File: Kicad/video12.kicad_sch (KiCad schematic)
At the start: 19 parts, among them J301 DE15HD, U301 THS7316, U302 TPD7S019

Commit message: Cleaned up the part numbers.
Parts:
- C301: Digikey 490-3886-1-ND -> (none); JLCPCB Collection (none) -> Basic; MPN GRM21BR61C106KE15L -> CL21A106KAYNNNE; Manufacturer Murata -> Samsung; Mouser 81-GRM21BR61C106KE15 -> (none); Voltage 10V -> 25V
- C302, C306: Digikey 399-C0805C104M5RAC7800CT-ND -> (none); JLCPCB Collection (none) -> Basic; MPN C0805C104M5RACTU -> CC0805KRX7R9BB104; Manufacturer Kemet -> Yageo; Mouser 80-C0805C104M5R -> (none); Tolerance X5R -> X7R; Voltage 10V -> 50V
- C303: Digikey 1276-1093-1-ND -> (none); JLCPCB Collection (none) -> Basic; Tolerance X5R -> X7R
- C304, C305: Digikey 399-C0805C104M5RAC7800CT-ND -> (none); JLCPCB Collection (none) -> Basic; MPN C0805C104M5RACTU -> CC0805KRX7R9BB104; Manufacturer Kemet -> Yageo; Mouser 80-C0805C104M5R -> (none); Tolerance X5R -> X7R; Voltage 16V -> 50V
- R301, R302, R303: Digikey RMCF0805FT75R0CT-ND -> (none); JLCPCB Collection (none) -> Basic; MPN RMCF0805FT75R0 -> 0805W8F750JT5E; Manufacturer Stackpole -> Uniroyal
- R305, R306: Digikey RMCF0805FT2K00CT-ND -> (none); JLCPCB Collection (none) -> Basic; MPN RMCF0805FT2K00 -> 0805W8F2001T5E; Manufacturer Stackpole -> Uniroyal
- U301: Digikey 296-26684-1-ND -> (none); JLCPCB Collection (none) -> Extended; MPN THS7316DR -> TPF133A; Manufacturer Texas Instruments -> 3PEAK; Mouser 595-THS7316DR -> (none)
- U302: Digikey 296-27595-1-ND -> (none); JLCPCB Collection (none) -> Extended; Mouser 595-TPD7S019-15DBQR -> (none)

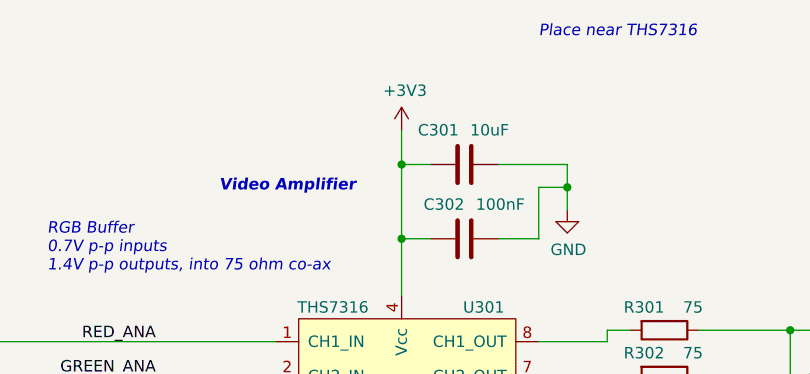
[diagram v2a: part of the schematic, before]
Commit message: Added a PC Speaker output.
To free up a BMC pin, the HDD LED is now driven from the I/O mux.
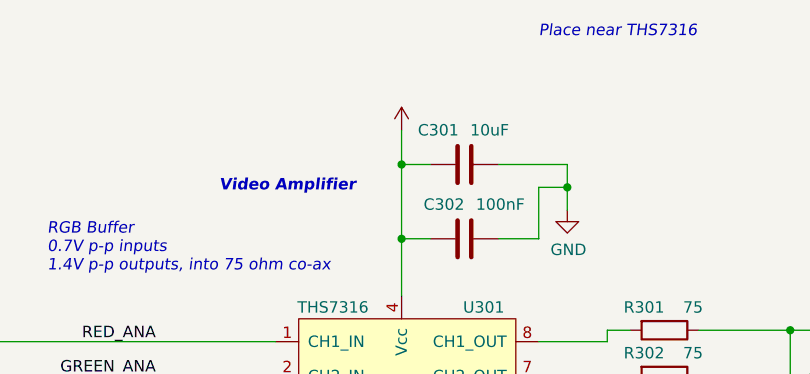
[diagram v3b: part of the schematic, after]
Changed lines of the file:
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@@
       (effects (font (size 1.27 1.27)) hide)
     )
-    (property "Value" "+3V3" (id 1) (at 110.871 41.9608 0))
+    (property "Value" "" (id 1) (at 110.871 41.9608 0))
     (property "Footprint" "" (id 2) (at 110.49 46.355 0)
       (effects (font (size 1.27 1.27)) hide)

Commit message: Label tweaks
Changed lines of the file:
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@@
       (effects (font (size 1.27 1.27)) hide)
     )
-    (property "Value" "" (id 1) (at 110.871 41.9608 0))
+    (property "Value" "+3V3" (id 1) (at 110.871 41.9608 0))
     (property "Footprint" "" (id 2) (at 110.49 46.355 0)
       (effects (font (size 1.27 1.27)) hide)

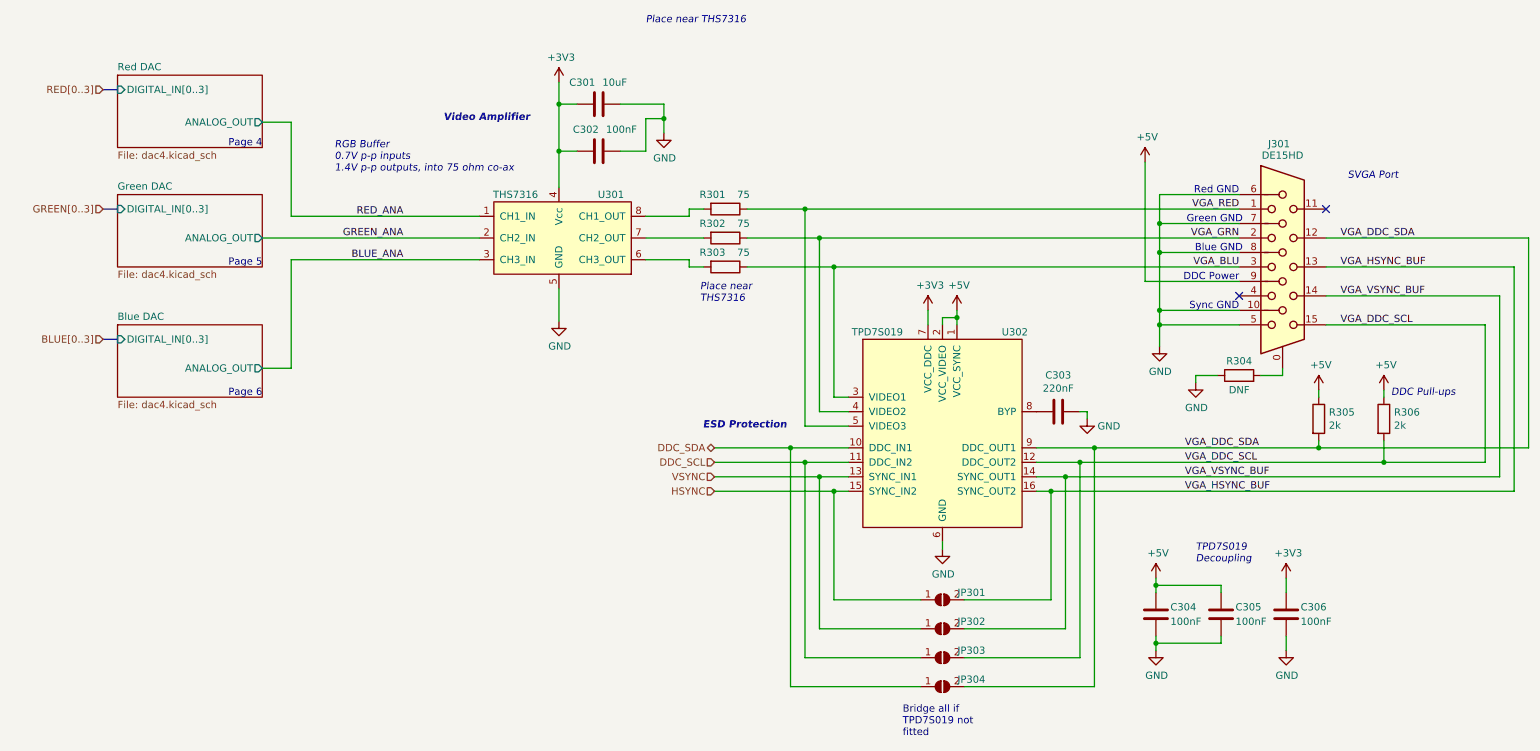
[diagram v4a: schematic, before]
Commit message: Replaced decoupling caps, and worked on PCB layout.
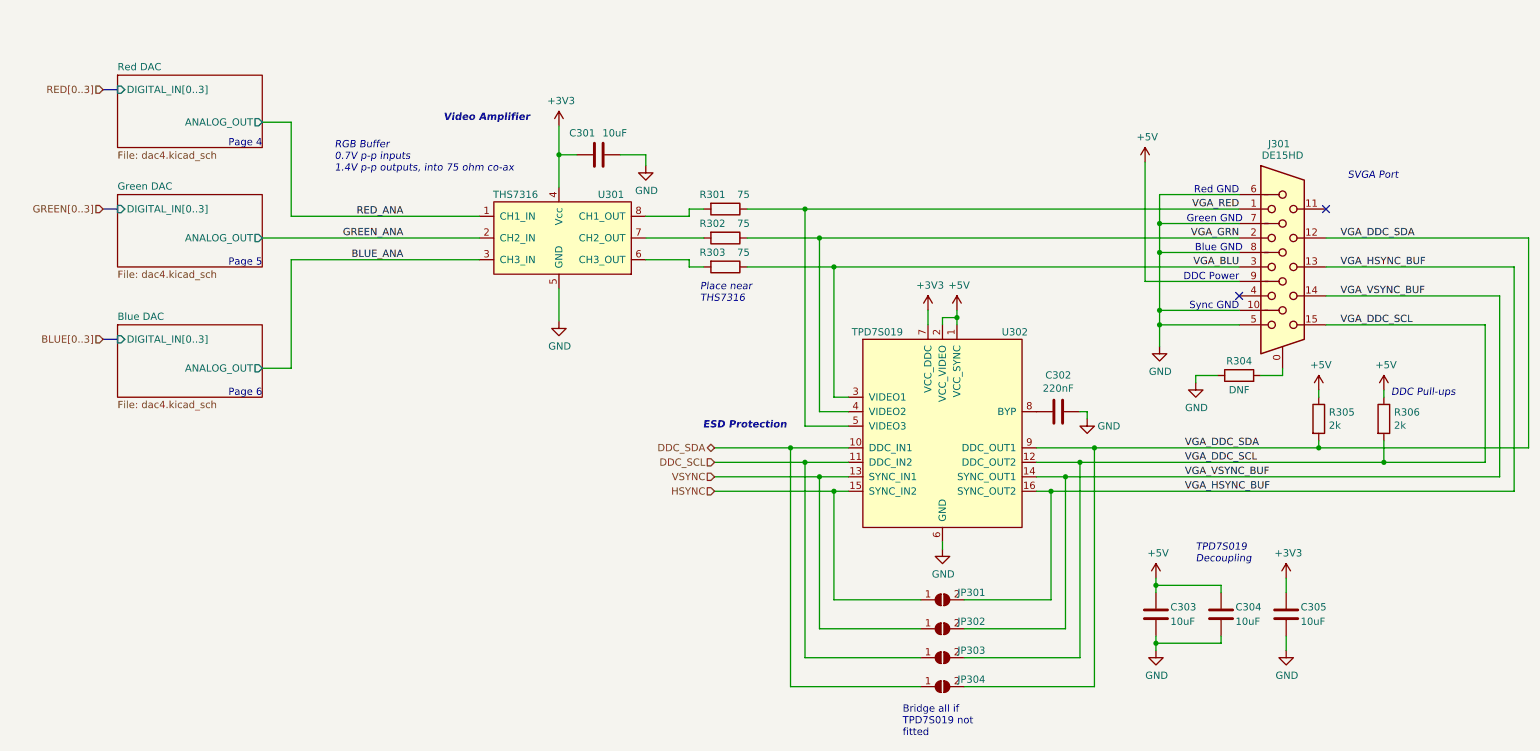
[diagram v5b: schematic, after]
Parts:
- removed C302, C306: 100nF, Capacitor_SMD:C_0805_2012Metric_Pad1.18x1.45mm_HandSolder, symbol Device:C
- added C303: 10uF, Capacitor_SMD:C_0805_2012Metric_Pad1.18x1.45mm_HandSolder, symbol Device:C
- C304, C305: value 100nF -> 10uF; LCSC Part# C49678 -> C15850; MPN CC0805KRX7R9BB104 -> CL21A106KAYNNNE; Manufacturer Yageo -> Samsung; Tolerance X7R -> X5R; Voltage 50V -> 25V
- renumbered C303 to C302
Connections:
- net +3V3: now also C305.2
- net +5V: now also C303.2; no longer C305.2
- net GND: now also C303.1
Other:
- moved on the sheet: C301

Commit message: Added source resistors on SPI bus.
Also renumbered pages.
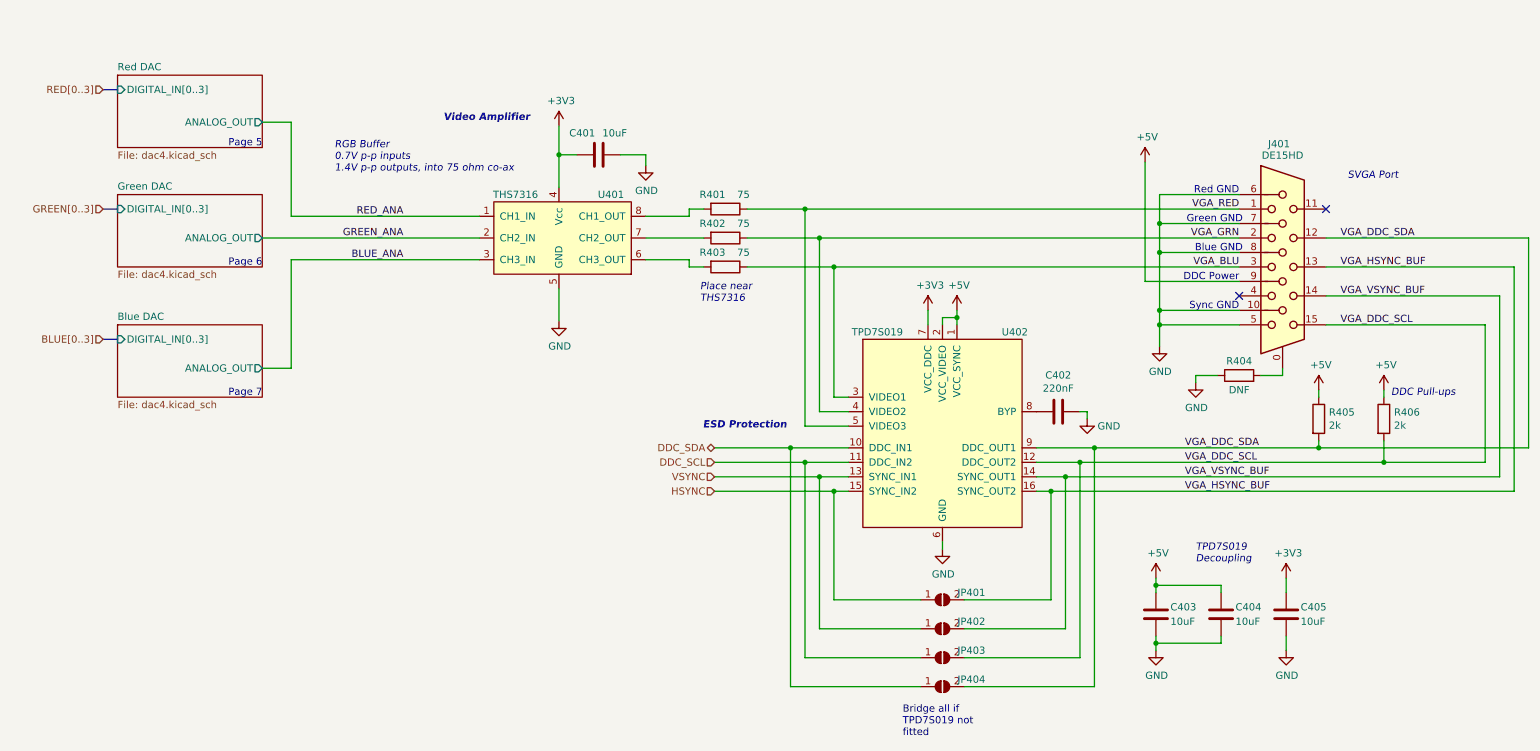
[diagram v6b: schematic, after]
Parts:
- renumbered C301 to C401, C302 to C402, C303 to C403, C304 to C404, C305 to C405, J301 to J401, JP301 to JP401, JP302 to JP402, JP303 to JP403, JP304 to JP404, R301 to R401, R302 to R402, R303 to R403, R304 to R404, R305 to R405, R306 to R406, U301 to U401, U302 to U402
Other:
- note added: "Page 7"
- note removed: "Page 4"

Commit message: Label adjustments.
Swap 10uF to 10u (the F is implied)
Adjust some left/right alignment and nudge some labels around
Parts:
- C401, C403, C404, C405: value 10uF -> 10u
- C402: value 220nF -> 220n
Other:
- moved on the sheet: C405
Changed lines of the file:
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@@
     (stroke (width 0) (type default) (color 0 0 0 0))
   )
-  (wire (pts (xy 238.125 135.89) (xy 238.125 133.35))
+  (wire (pts (xy 239.395 135.89) (xy 239.395 133.35))
     (stroke (width 0) (type default) (color 0 0 0 0))
   )
@@
     (stroke (width 0) (type default) (color 0 0 0 0))
   )
-  (wire (pts (xy 238.125 146.05) (xy 238.125 143.51))
+  (wire (pts (xy 239.395 146.05) (xy 239.395 143.51))
     (stroke (width 0) (type default) (color 0 0 0 0))
   )
@@
       (effects (font (size 1.27 1.27)) (justify left))
     )
-    (property "Value" "10uF" (id 1) (at 118.11 55.245 90)
+    (property "Value" "10u" (id 1) (at 118.11 55.245 90)
       (effects (font (size 1.27 1.27)) (justify right))
     )
@@
     (pin "2")
   )
-  (symbol (lib_id "power:+3V3") (at 238.125 133.35 0) (unit 1)
-    (in_bom yes) (on_board yes)
-    (property "Reference" "#PWR0414" (id 0) (at 238.125 137.16 0)
-      (effects (font (size 1.27 1.27)) hide)
-    )
-    (property "Value" "+3V3" (id 1) (at 238.506 128.9558 0))
-    (property "Footprint" "" (id 2) (at 238.125 133.35 0)
-      (effects (font (size 1.27 1.27)) hide)
-    )
-    (property "Datasheet" "" (id 3) (at 238.125 133.35 0)
+  (symbol (lib_id "power:+3V3") (at 239.395 133.35 0) (unit 1)
+    (in_bom yes) (on_board yes)
+    (property "Reference" "#PWR0414" (id 0) (at 239.395 137.16 0)
+      (effects (font (size 1.27 1.27)) hide)
+    )
+    (property "Value" "+3V3" (id 1) (at 239.776 128.9558 0))
+    (property "Footprint" "" (id 2) (at 239.395 133.35 0)
+      (effects (font (size 1.27 1.27)) hide)
+    )
+    (property "Datasheet" "" (id 3) (at 239.395 133.35 0)
       (effects (font (size 1.27 1.27)) hide)
     )
@@
     (in_bom yes) (on_board yes)
     (property "Reference" "C402" (id 0) (at 198.12 97.7392 90))
-    (property "Value" "220nF" (id 1) (at 198.12 100.0506 90))
+    (property "Value" "220n" (id 1) (at 198.12 100.0506 90))
     (property "Footprint" "Capacitor_SMD:C_0805_2012Metric_Pad1.18x1.45mm_HandSolder" (id 2) (at 194.31 105.1052 0)
       (effects (font (size 1.27 1.27)) hide)
@@
     (pin "1")
   )
-  (symbol (lib_id "power:GND") (at 238.125 146.05 0) (unit 1)
-    (in_bom yes) (on_board yes)
-    (property "Reference" "#PWR0416" (id 0) (at 238.125 152.4 0)
-      (effects (font (size 1.27 1.27)) hide)
-    )
-    (property "Value" "GND" (id 1) (at 238.252 150.4442 0))
-    (property "Footprint" "" (id 2) (at 238.125 146.05 0)
-      (effects (font (size 1.27 1.27)) hide)
-    )
-    (property "Datasheet" "" (id 3) (at 238.125 146.05 0)
+  (symbol (lib_id "power:GND") (at 239.395 146.05 0) (unit 1)
+    (in_bom yes) (on_board yes)
+    (property "Reference" "#PWR0416" (id 0) (at 239.395 152.4 0)
+      (effects (font (size 1.27 1.27)) hide)
+    )
+    (property "Value" "GND" (id 1) (at 239.522 150.4442 0))
+    (property "Footprint" "" (id 2) (at 239.395 146.05 0)
+      (effects (font (size 1.27 1.27)) hide)
+    )
+    (property "Datasheet" "" (id 3) (at 239.395 146.05 0)
       (effects (font (size 1.27 1.27)) hide)
     )
@@
       (effects (font (size 1.27 1.27)) (justify left))
     )
-    (property "Value" "10uF" (id 1) (at 217.805 140.97 0)
+    (property "Value" "10u" (id 1) (at 217.805 140.97 0)
       (effects (font (size 1.27 1.27)) (justify left))
     )
@@
     (pin "2")
   )
-  (symbol (lib_id "Device:C") (at 238.125 139.7 0) (mirror x) (unit 1)
-    (in_bom yes) (on_board yes)
-    (property "Reference" "C405" (id 0) (at 240.665 138.43 0)
+  (symbol (lib_id "Device:C") (at 239.395 139.7 0) (mirror x) (unit 1)
+    (in_bom yes) (on_board yes)
+    (property "Reference" "C405" (id 0) (at 241.935 138.43 0)
       (effects (font (size 1.27 1.27)) (justify left))
     )
-    (property "Value" "10uF" (id 1) (at 240.665 140.97 0)
+    (property "Value" "10u" (id 1) (at 241.935 140.97 0)
       (effects (font (size 1.27 1.27)) (justify left))
     )
-    (property "Footprint" "Capacitor_SMD:C_0805_2012Metric_Pad1.18x1.45mm_HandSolder" (id 2) (at 239.0902 135.89 0)
-      (effects (font (size 1.27 1.27)) hide)
-    )
-    (property "Datasheet" "~" (id 3) (at 238.125 139.7 0)
-      (effects (font (size 1.27 1.27)) hide)
-    )
-    (property "DNP" "0" (id 4) (at 238.125 139.7 0)
-      (effects (font (size 1.27 1.27)) hide)
-    )
-    (property "Digikey" "~" (id 5) (at 238.125 139.7 0)
-      (effects (font (size 1.27 1.27)) hide)
-    )
-    (property "MPN" "CL21A106KAYNNNE" (id 6) (at 238.125 139.7 0)
-      (effects (font (size 1.27 1.27)) hide)
-    )
-    (property "Manufacturer" "Samsung" (id 7) (at 238.125 139.7 0)
-      (effects (font (size 1.27 1.27)) hide)
-    )
-    (property "LCSC Part#" "C15850" (id 8) (at 238.125 139.7 0)
-      (effects (font (size 1.27 1.27)) hide)
-    )
-    (property "Tolerance" "X5R" (id 9) (at 238.125 139.7 0)
-      (effects (font (size 1.27 1.27)) hide)
-    )
-    (property "Voltage" "25V" (id 10) (at 238.125 139.7 0)
-      (effects (font (size 1.27 1.27)) hide)
-    )
-    (property "Mouser" "~" (id 11) (at 238.125 139.7 0)
-      (effects (font (size 1.27 1.27)) hide)
-    )
-    (property "JLCPCB Collection" "Basic" (id 12) (at 238.125 139.7 0)
+    (property "Footprint" "Capacitor_SMD:C_0805_2012Metric_Pad1.18x1.45mm_HandSolder" (id 2) (at 240.3602 135.89 0)
+      (effects (font (size 1.27 1.27)) hide)
+    )
+    (property "Datasheet" "~" (id 3) (at 239.395 139.7 0)
+      (effects (font (size 1.27 1.27)) hide)
+    )
+    (property "DNP" "0" (id 4) (at 239.395 139.7 0)
+      (effects (font (size 1.27 1.27)) hide)
+    )
+    (property "Digikey" "~" (id 5) (at 239.395 139.7 0)
+      (effects (font (size 1.27 1.27)) hide)
+    )
+    (property "MPN" "CL21A106KAYNNNE" (id 6) (at 239.395 139.7 0)
+      (effects (font (size 1.27 1.27)) hide)
+    )
+    (property "Manufacturer" "Samsung" (id 7) (at 239.395 139.7 0)
+      (effects (font (size 1.27 1.27)) hide)
+    )
+    (property "LCSC Part#" "C15850" (id 8) (at 239.395 139.7 0)
+      (effects (font (size 1.27 1.27)) hide)
+    )
+    (property "Tolerance" "X5R" (id 9) (at 239.395 139.7 0)
+      (effects (font (size 1.27 1.27)) hide)
+    )
+    (property "Voltage" "25V" (id 10) (at 239.395 139.7 0)
+      (effects (font (size 1.27 1.27)) hide)
+    )
+    (property "Mouser" "~" (id 11) (at 239.395 139.7 0)
+      (effects (font (size 1.27 1.27)) hide)
+    )
+    (property "JLCPCB Collection" "Basic" (id 12) (at 239.395 139.7 0)
       (effects (font (size 1.27 1.27)) hide)
     )
@@
       (effects (font (size 1.27 1.27)) (justify left))
     )
-    (property "Value" "10uF" (id 1) (at 229.235 140.97 0)
+    (property "Value" "10u" (id 1) (at 229.235 140.97 0)
       (effects (font (size 1.27 1.27)) (justify left))
     )

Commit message: Swap video buffer to DIO2663
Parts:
- U401: value THS7316 -> DIO2663; LCSC Part# C155446 -> C444598; MPN TPF133A -> DIO2663; Manufacturer 3PEAK -> DIOO
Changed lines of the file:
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@@
       (effects (font (size 1.27 1.27)) (justify right))
     )
-    (property "Value" "THS7316" (id 1) (at 102.87 66.04 0))
+    (property "Value" "DIO2663" (id 1) (at 102.87 66.04 0))
     (property "Footprint" "Package_SO:SOIC-8_3.9x4.9mm_P1.27mm" (id 2) (at 114.3 87.63 0)
       (effects (font (size 2.54 2.54)) hide)
     )
-    (property "Datasheet" "https://datasheet.lcsc.com/szlcsc/1810181731_3PEAK-TPF133A-SR_C155446.pdf" (id 3) (at 96.52 74.93 0)
+    (property "Datasheet" "https://datasheet.lcsc.com/lcsc/2203091604_DIOO-DIO2663CS8_C444605.pdf" (id 3) (at 96.52 74.93 0)
       (effects (font (size 2.54 2.54)) hide)
     )
-    (property "Manufacturer" "3PEAK" (id 4) (at 116.84 66.04 0)
+    (property "Manufacturer" "DIOO" (id 4) (at 116.84 66.04 0)
       (effects (font (size 1.27 1.27)) hide)
     )
@@
       (effects (font (size 1.27 1.27)) hide)
     )
-    (property "MPN" "TPF133A" (id 7) (at 114.3 73.66 0)
+    (property "MPN" "DIO2663" (id 7) (at 114.3 73.66 0)
       (effects (font (size 1.27 1.27)) hide)
     )
@@
       (effects (font (size 1.27 1.27)) hide)
     )
-    (property "LCSC Part#" "C155446" (id 9) (at 114.3 73.66 0)
+    (property "LCSC Part#" "C444598" (id 9) (at 114.3 73.66 0)
       (effects (font (size 1.27 1.27)) hide)
     )
